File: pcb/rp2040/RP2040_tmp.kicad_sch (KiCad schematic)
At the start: 36 parts, among them J0 USB_C_Receptacle_USB2.0, J1 BREAKOUT, J2 Conn_01x03_Male, SW0 RESET, SW2 RESET, U1 NCP1117-3.3 larger footprint,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, U2 W25Q128JVS, U3 RP2040, U44 SRV05-4, Y0 12MHZ Crystal

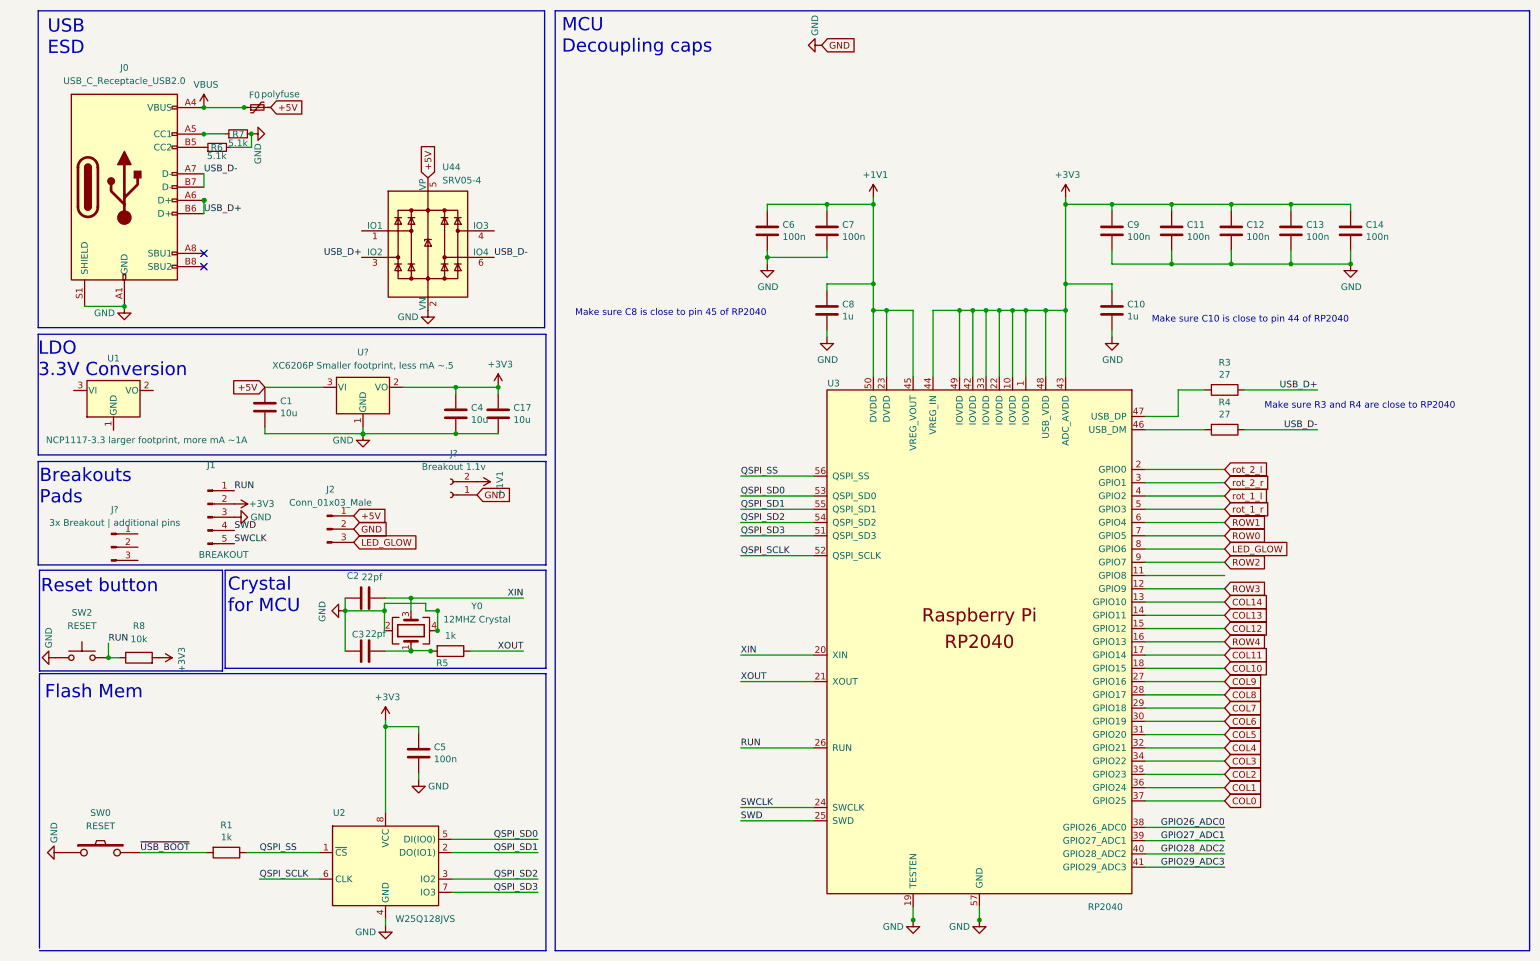
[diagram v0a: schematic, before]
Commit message: diode positioning done
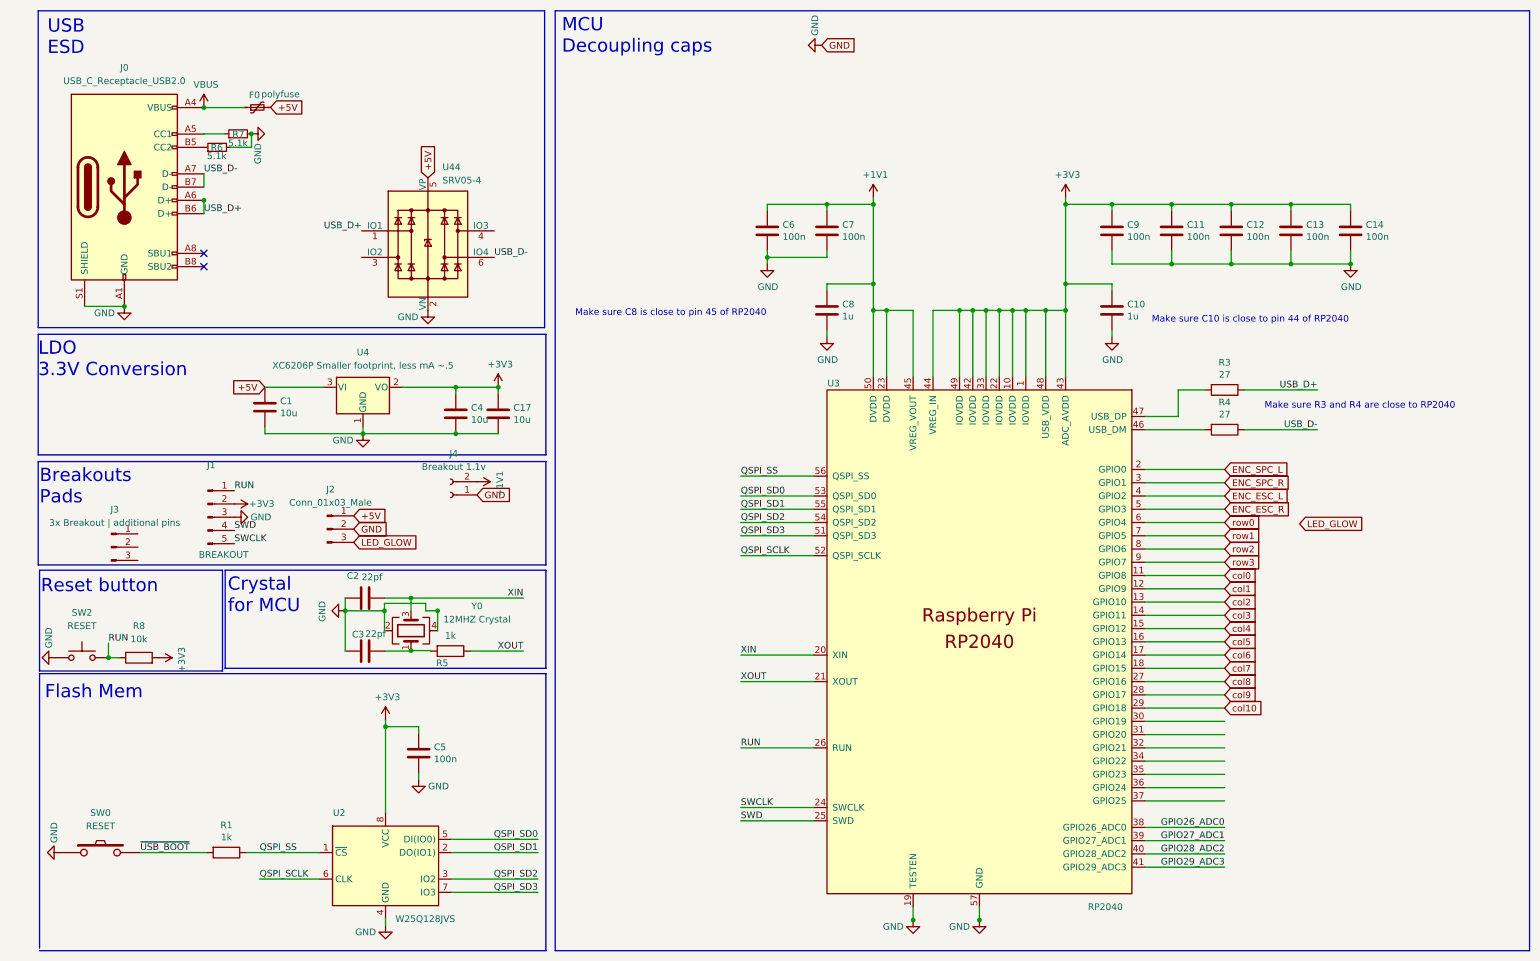
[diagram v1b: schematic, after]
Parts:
- removed U1: NCP1117-3.3 larger footprint, more mA ~1A, Package_TO_SOT_SMD:SOT-223-3_TabPin2, symbol Regulator_Linear:NCP1117-3.3_SOT223
- J2: footprint Connector_PinSocket_1.27mm:PinSocket_1x03_P1.27mm_Vertical -> Connector_PinSocket_2.54mm:PinSocket_1x03_P2.54mm_Vertical
- J3: renamed from J?; footprint Connector_PinHeader_2.54mm:PinHeader_1x03_P2.54mm_Vertical -> Connector_PinSocket_2.54mm:PinSocket_1x03_P2.54mm_Vertical
- J4: renamed from J?; footprint Connector_PinHeader_2.54mm:PinHeader_1x02_P2.54mm_Vertical -> Connector_PinSocket_2.54mm:PinSocket_1x02_P2.54mm_Vertical
- gave numbers to parts that had none: 1
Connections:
- net LED_GLOW: no longer U3.8 (GPIO6)
- net USB_D+: now also U44.1 (IO1); no longer U44.3 (IO2)
- net col0: now reaches U3.11 (GPIO8)
- net COL0: no longer names the net of U3.37 (GPIO25)
- net COL1: no longer names the net of U3.36 (GPIO24)
- net COL10 renamed col7
- net COL11 renamed col6
- net COL12 renamed col4
- net COL13 renamed col3
- net COL14 renamed col2
- net COL2: no longer names the net of U3.35 (GPIO23)
- net COL3: no longer names the net of U3.34 (GPIO22)
- net COL4: no longer names the net of U3.32 (GPIO21)
- net COL5: no longer names the net of U3.31 (GPIO20)
- net COL6: no longer names the net of U3.30 (GPIO19)
- net COL7 renamed col10
- net COL8 renamed col9
- net COL9 renamed col8
- net ROW0 renamed row1
- net ROW1 renamed row0
- net ROW2 renamed row3
- net ROW3 renamed col1
- net ROW4 renamed col5
- net rot_1_l renamed ENC_ESC_L
- net rot_1_r renamed ENC_ESC_R
- net rot_2_l renamed ENC_SPC_L
- net rot_2_r renamed ENC_SPC_R
- new net row2: U3.8 (GPIO6)

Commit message: finalized routing, placement of components
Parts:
- removed J3: 3x Breakout | additional pins, Connector_PinSocket_2.54mm:PinSocket_1x03_P2.54mm_Vertical, symbol Connector:Conn_01x03_Male
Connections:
- net col10 is gone; now on net ENC_ESC_L: U3.29 (GPIO18)
- net col9 is gone; now on net ENC_ESC_R: U3.28 (GPIO17)
- net row0 is gone; now on net ENC_SPC_L: U3.6 (GPIO4)
- net row1 is gone; now on net ENC_SPC_R: U3.7 (GPIO5)
- net ENC_ESC_L: no longer U3.4 (GPIO2)
- net ENC_ESC_R: no longer U3.5 (GPIO3)
- net ENC_SPC_L: no longer U3.2 (GPIO0)
- net ENC_SPC_R: no longer U3.3 (GPIO1)
- net GND: now also J1.1 (Pin_1); no longer J1.3 (Pin_3)
- net LED_GLOW: now also U3.36 (GPIO24)
- net RUN: now also J1.3 (Pin_3); no longer J1.1 (Pin_1)
- net ROW0: now reaches U3.30 (GPIO19)
- net ROW1: now reaches U3.35 (GPIO23)
- net COL11: now reaches U3.37 (GPIO25)
- net col0 renamed COL2
- net col1 renamed COL3
- net col2 renamed COL4
- net col3 renamed COL5
- net col4 renamed COL6
- net col5 renamed COL7
- net col6 renamed COL8
- net col7 renamed COL9
- net col8: no longer names the net of U3.27 (GPIO16)
- net row2 renamed COL0
- net row3 renamed COL1
- new net COL10: U3.5 (GPIO3)
- new net RGB: U3.3 (GPIO1)
- new net ROW2: U3.4 (GPIO2)
- new net ROW3: U3.2 (GPIO0)
